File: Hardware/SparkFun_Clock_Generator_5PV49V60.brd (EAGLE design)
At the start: 27.9 x 25.4 mm, 74 parts, among them U1 IDT_5P49V60_CLOCK_GENERATOR, Y1 16MHz

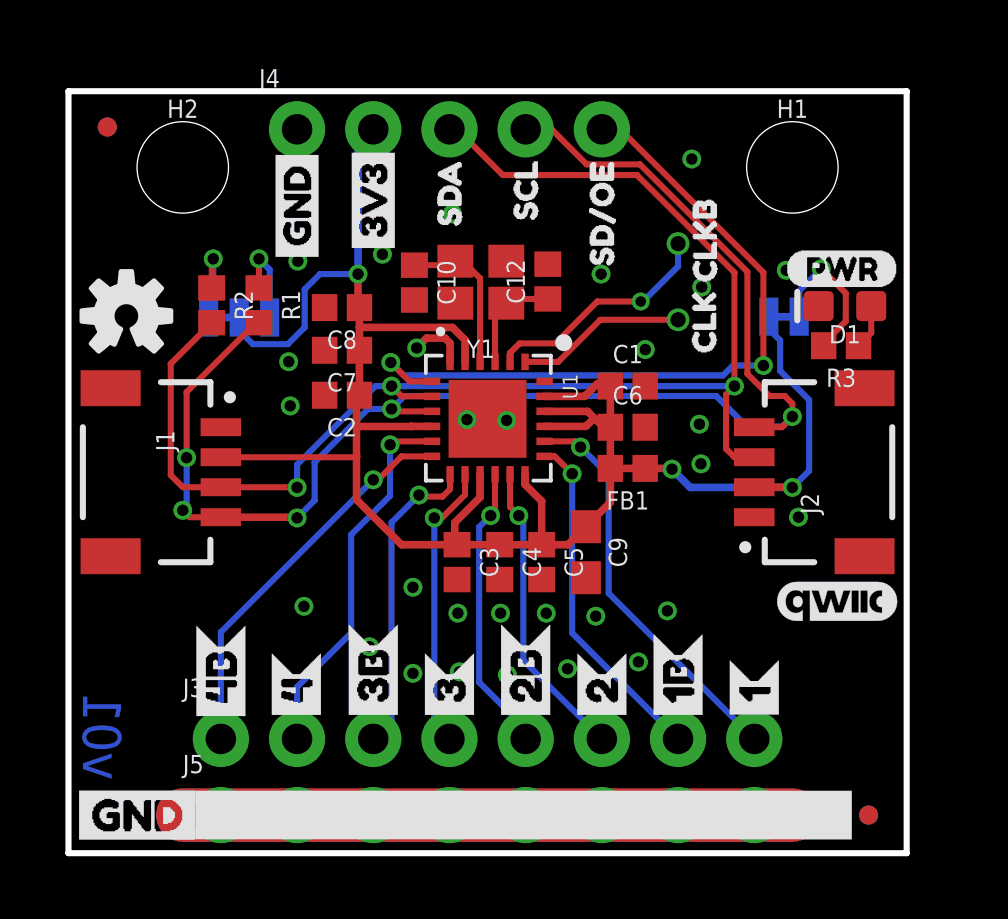
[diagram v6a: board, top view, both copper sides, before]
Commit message: Adds default address to schematic, moves design to 0,0 , updates right angle qwiic connector with value
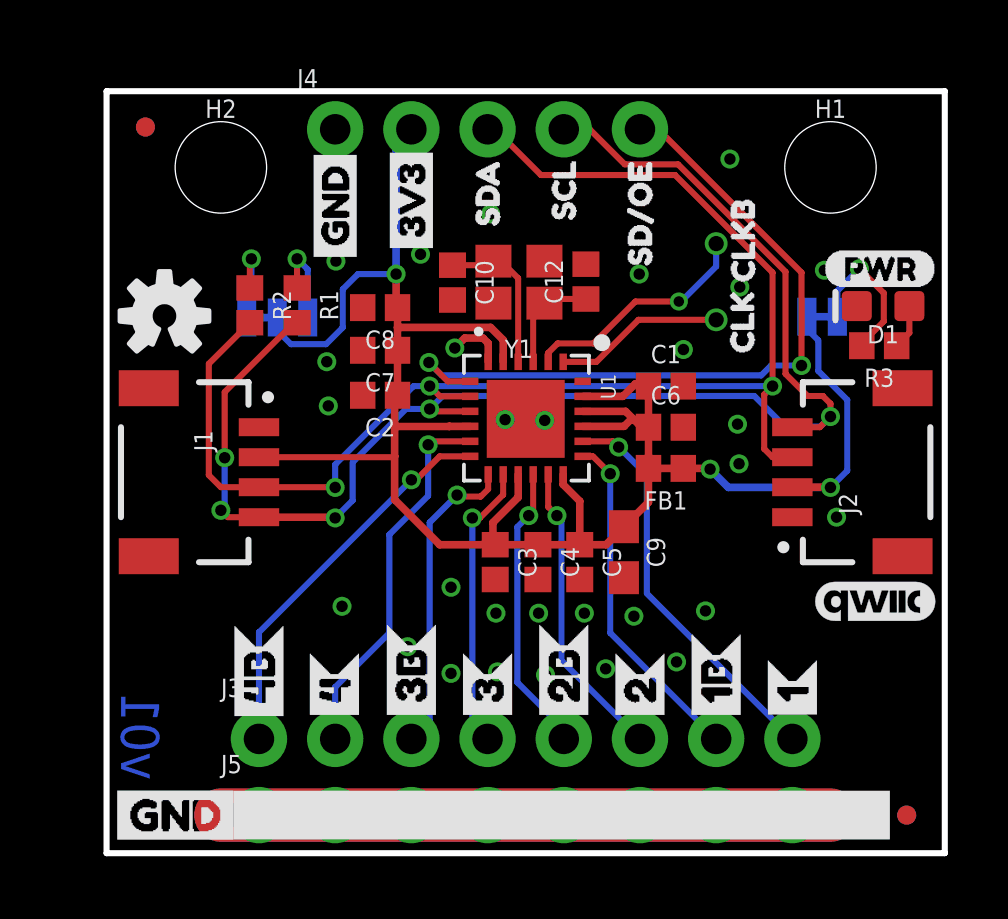
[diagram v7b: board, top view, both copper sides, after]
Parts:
- J1, J2: value (none) -> QWIIC_RIGHT_ANGLE
- moved FD3 1.27 mm to (26.7, 1.27)
- moved FD4 1.27 mm to (26.7, 1.27)
- moved C3 1.27 mm to (13.0, 9.70)
- moved C5 1.27 mm to (15.8, 9.70)
- moved C9 1.27 mm to (17.2, 10.0)
- moved LOGO1 1.27 mm to (14.0, 15.2)
- moved U1 1.27 mm to (14.0, 14.5)
- moved Y1 1.27 mm to (13.7, 19.0)
- moved C2 1.27 mm to (9.12, 15.3)
- moved C7 1.27 mm to (9.12, 16.8)
- moved C8 1.27 mm to (9.12, 18.2)
- moved J4 1.27 mm to (7.62, 24.1)
- moved JP1 1.27 mm to (5.69, 17.9)
- moved U$15 1.27 mm to (7.62, 9.42)
- moved U$19 1.27 mm to (7.62, 23.7)
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
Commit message: Changes DRC to SparkFun Tight to ensure that JLCPCB could do it - parts were adjusted accordingly
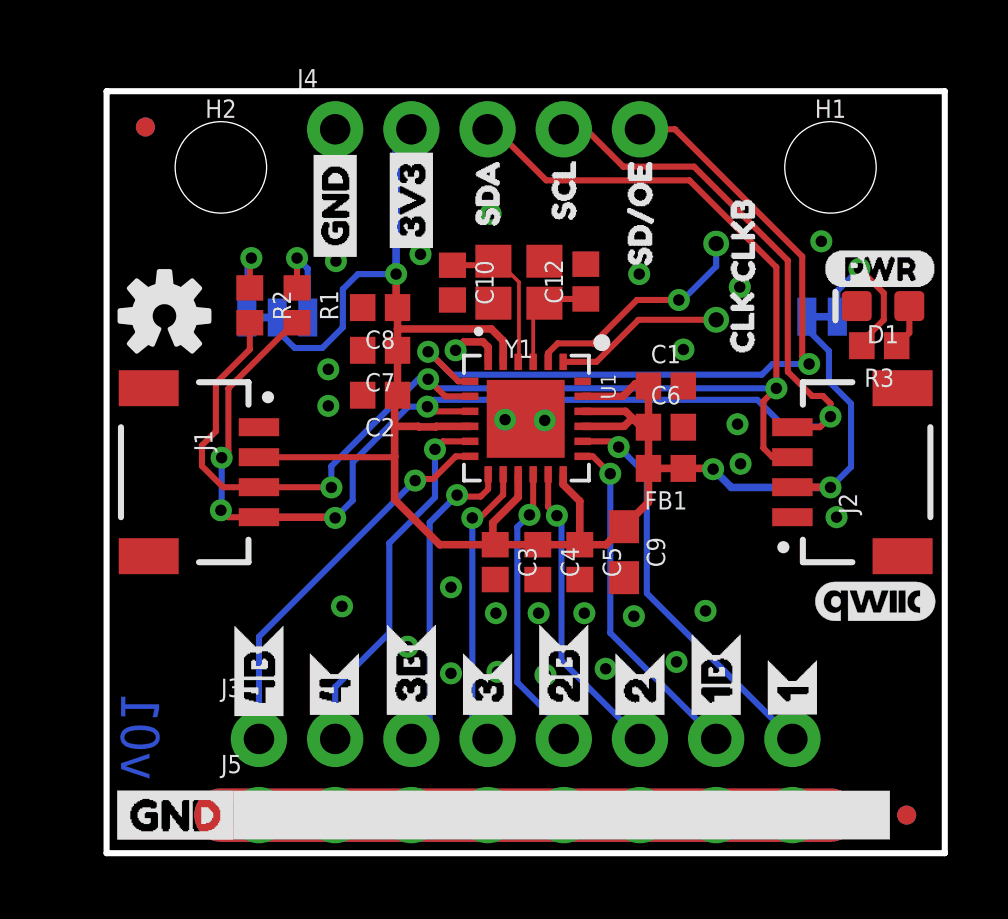
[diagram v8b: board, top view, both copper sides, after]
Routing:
- net SD/OE: track 24.8 -> 25.8 mm
- net SEL1/SDA: track 46.5 -> 47.4 mm
- net GND: track 42.6 -> 42.4 mm, vias 29 -> 28
